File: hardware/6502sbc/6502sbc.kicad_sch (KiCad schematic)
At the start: 1 part, among them U1 W65C02SxP

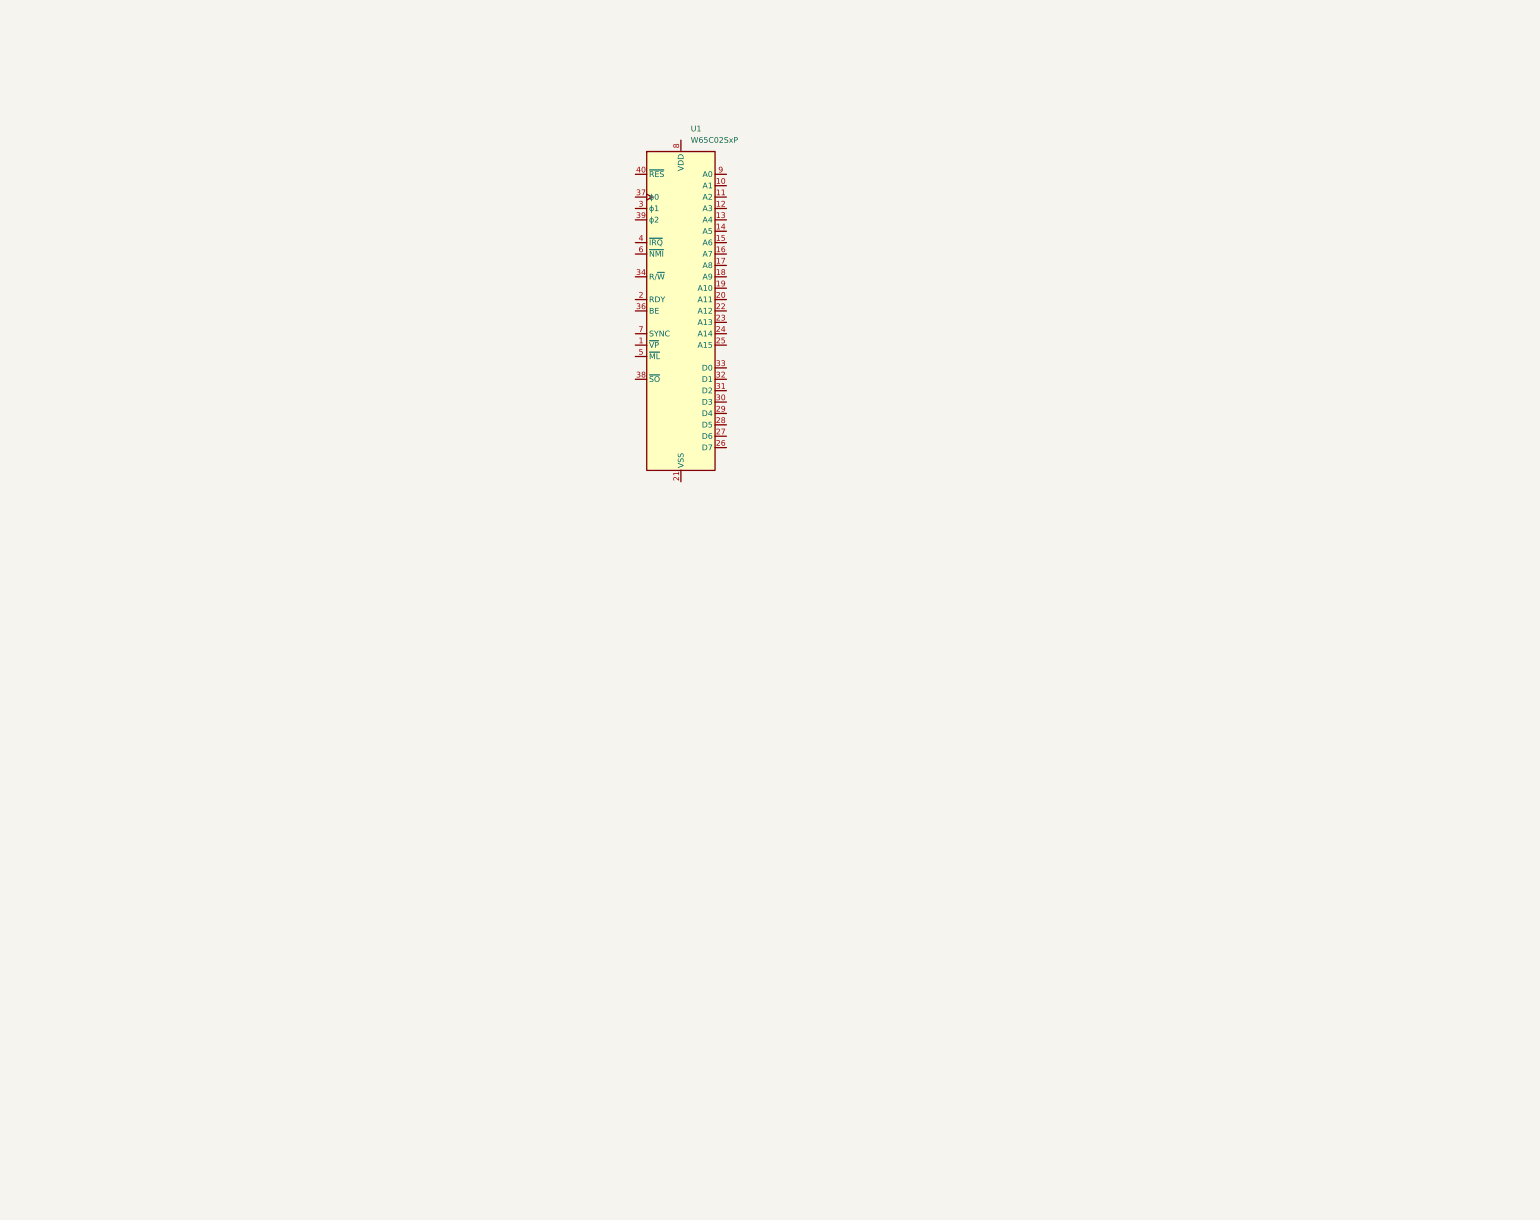
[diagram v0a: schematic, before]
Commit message: KiCAD schematic is mostly complete
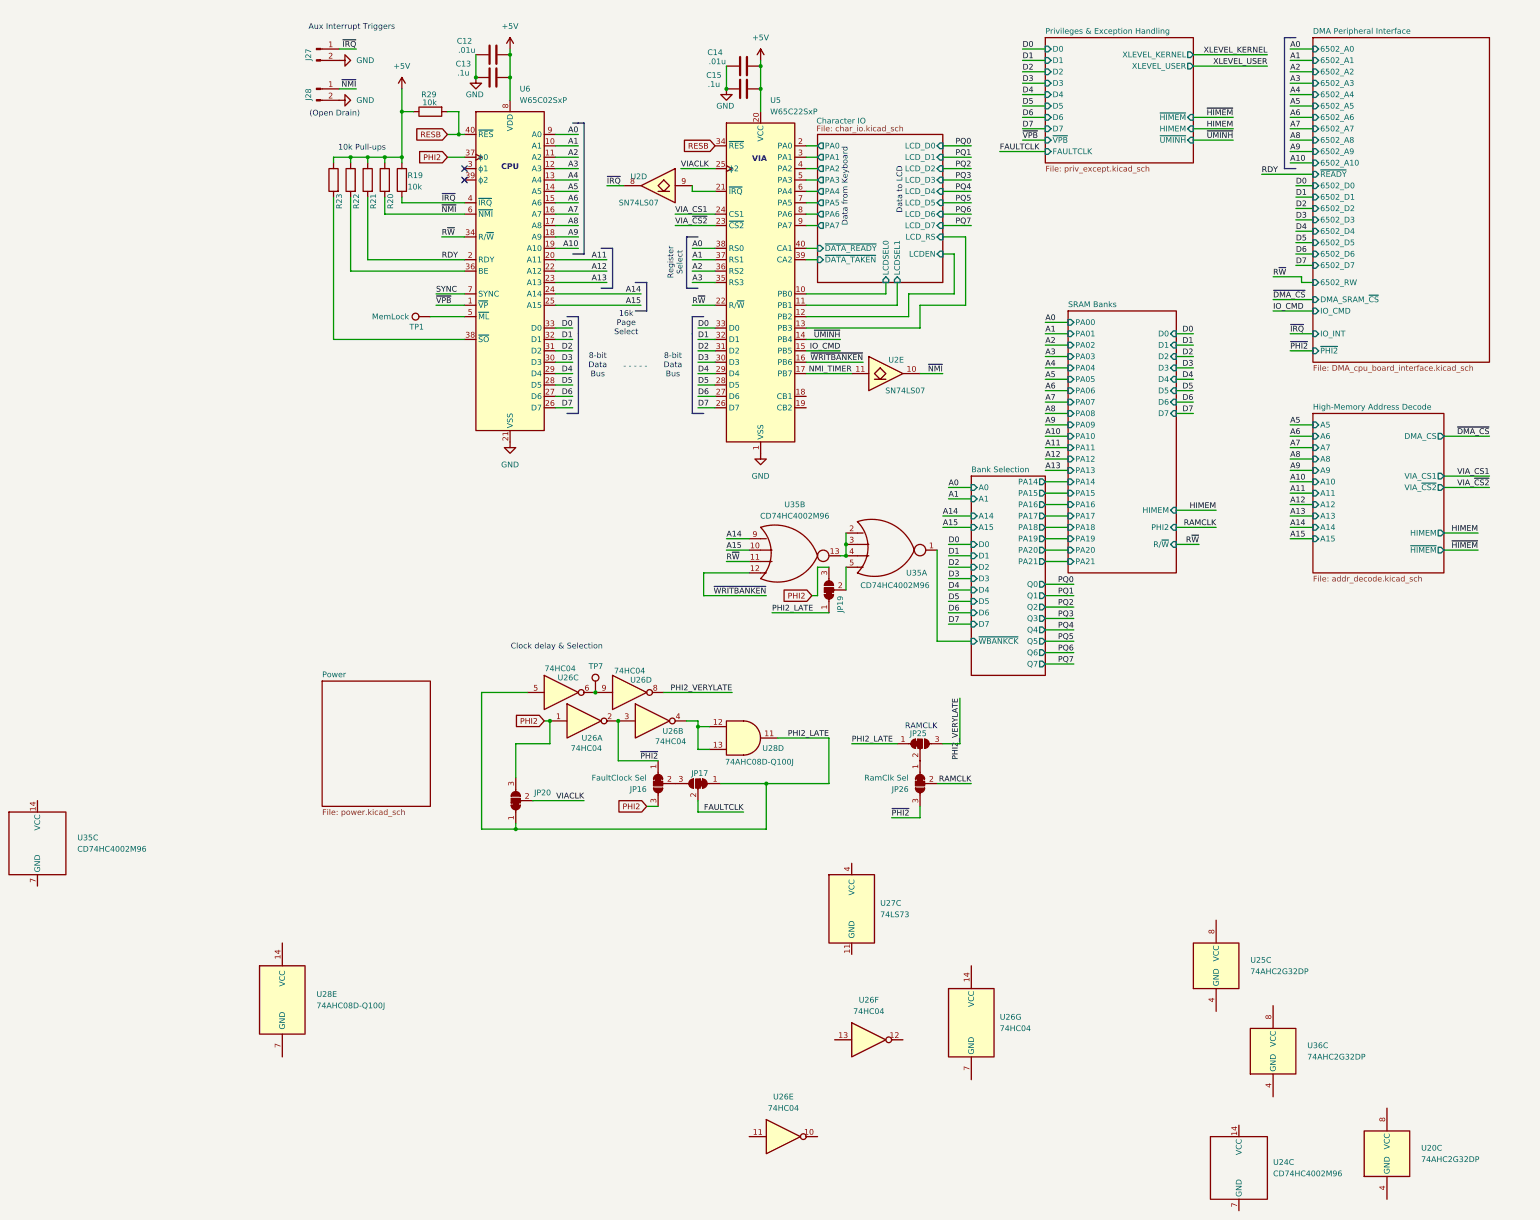
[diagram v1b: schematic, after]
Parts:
- removed U1: W65C02SxP, Package_DIP:DIP-40_W15.24mm, symbol PCM_65xx-library:W65C02SxP
- added C12, C14: .01u, symbol Device:C
- added C13, C15: .1u, symbol Device:C
- added J27, J28: Conn_01x02_Pin, symbol Connector:Conn_01x02_Pin
- added JP16, JP17, JP25: FaultClock Sel, symbol Jumper:SolderJumper_3_Bridged12
- added JP19, JP20: SolderJumper_3_Bridged12, symbol Jumper:SolderJumper_3_Bridged12
- added JP26: RamClk Sel, symbol Jumper:SolderJumper_3_Bridged12
- added R19, R20, R21, R22, R23, R29: 10k, symbol Device:R
- added TP1: MemLock, symbol Connector:TestPoint
- added TP7: TestPoint, symbol Connector:TestPoint
- added U2: SN74LS07, symbol 74xx:SN74LS07
- added U20, U25, U36: 74AHC2G32DP, symbol 74xGxx:74LVC2G32
- added U24, U35: CD74HC4002M96, Package_SO:SOIC-14_3.9x8.7mm_P1.27mm, symbol custom:_1
- added U26: 74HC04, symbol 74xx:74HC04
- added U27: 74LS73, symbol 74xx:74LS73
- added U28: 74AHC08D-Q100J, symbol 74xx:74LS08
- added U5: W65C22SxP, Package_DIP:DIP-40_W15.24mm, symbol PCM_65xx-library:W65C22SxP
- added U6: W65C02SxP, Package_DIP:DIP-40_W15.24mm, symbol PCM_65xx-library:W65C02SxP
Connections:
- new net: TP7.1, U26.6, U26.9
- new net: JP16.2 (C), JP17.3 (B)
- new net: JP25.2 (C), JP26.1 (A)
- new net: R23.2, U6.38 (~{SO})
- new net: U35.13, U35.2, U35.3, U35.4
- new net: U2.9, U5.21 (~{IRQ})
- new net: R22.2, U6.36 (BE)
- new net: TP1.1, U6.5 (~{ML})
- new net: JP19.2 (C), U35.5
- new net: U26.4, U28.12, U28.13
- new net +5V: C12.1, C13.1, C14.1, C15.1, R19.1, R20.1, R21.1, R22.1, R23.1, R29.1, U5.20 (VCC), U6.8 (VDD)
- new net A0: U5.38 (RS0), U6.9 (A0)
- new net A1: U5.37 (RS1), U6.10 (A1)
- new net A10: U6.19 (A10)
- new net A11: U6.20 (A11)
- new net A12: U6.22 (A12)
- new net A13: U6.23 (A13)
- new net A14: U35.9, U6.24 (A14)
- new net A15: U35.10, U6.25 (A15)
- new net A2: U5.36 (RS2), U6.11 (A2)
- new net A3: U5.35 (RS3), U6.12 (A3)
- new net A4: U6.13 (A4)
- new net A5: U6.14 (A5)
- new net A6: U6.15 (A6)
- new net A7: U6.16 (A7)
- new net A8: U6.17 (A8)
- new net A9: U6.18 (A9)
- new net Bank Selection/~{WBANKCK}: U35.1
- new net Character IO/LCDEN: U5.12 (PB2)
- new net Character IO/LCDSEL0: U5.10 (PB0)
- new net Character IO/LCDSEL1: U5.11 (PB1)
- new net Character IO/LCD_RS: U5.13 (PB3)
- new net Character IO/PA0: U5.2 (PA0)
- new net Character IO/PA1: U5.3 (PA1)
- new net Character IO/PA2: U5.4 (PA2)
- new net Character IO/PA3: U5.5 (PA3)
- new net Character IO/PA4: U5.6 (PA4)
- new net Character IO/PA5: U5.7 (PA5)
- new net Character IO/PA6: U5.8 (PA6)
- new net Character IO/PA7: U5.9 (PA7)
- new net Character IO/~{DATA_READY}: U5.40 (CA1)
- new net Character IO/~{DATA_TAKEN}: U5.39 (CA2)
- new net D0: U5.33 (D0), U6.33 (D0)
- new net D1: U5.32 (D1), U6.32 (D1)
- new net D2: U5.31 (D2), U6.31 (D2)
- new net D3: U5.30 (D3), U6.30 (D3)
- new net D4: U5.29 (D4), U6.29 (D4)
- new net D5: U5.28 (D5), U6.28 (D5)
- new net D6: U5.27 (D6), U6.27 (D6)
- new net D7: U5.26 (D7), U6.26 (D7)
- new net FAULTCLK: JP17.2 (C)
- new net GND: C12.2, C13.2, C14.2, C15.2, J27.2 (Pin_2), J28.2 (Pin_2), U5.1 (VSS), U6.21 (VSS)
- new net IO_CMD: U5.15 (PB5)
- new net NMI_TIMER: U2.11, U5.17 (PB7)
- new net PHI2: JP16.3 (B), JP19.3 (B), JP20.3 (B), U26.1, U6.37 (ϕ0)
- new net PHI2_LATE: JP17.1 (A), JP19.1 (A), JP20.1 (A), JP25.1 (A), U26.5, U28.11
- new net PHI2_VERYLATE: JP25.3 (B), U26.8
- new net RAMCLK: JP26.2 (C)
- new net RDY: R21.2, U6.2 (RDY)
- new net RESB: R29.2, U5.34 (~{RES}), U6.40 (~{RES})
- new net R~{W}: U35.11, U5.22 (R/~{W}), U6.34 (R/~{W})
- new net SYNC: U6.7 (SYNC)
- new net VIACLK: JP20.2 (C), U5.25 (ϕ2)
- new net VIA_CS1: U5.24 (CS1)
- new net VIA_~{CS2}: U5.23 (~{CS2})
- new net ~{IRQ}: J27.1 (Pin_1), R19.2, U2.8, U6.4 (~{IRQ})
- new net ~{NMI}: J28.1 (Pin_1), R20.2, U2.10, U6.6 (~{NMI})
- new net ~{PHI2}: JP16.1 (A), JP26.3 (B), U26.2, U26.3
- new net ~{UMINH}: U5.14 (PB4)
- new net ~{VPB}: U6.1 (~{VP})
- new net ~{WRITBANKEN}: U35.12, U5.16 (PB6)
- no-connect marks 0 -> 2
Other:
- added sheet Bank Selection (bank_sel.kicad_sch)
- added sheet Character IO (char_io.kicad_sch)
- added sheet DMA Peripheral Interface (DMA_cpu_board_interface.kicad_sch)
- added sheet High-Memory Address Decode (addr_decode.kicad_sch)
- added sheet Power (power.kicad_sch)
- added sheet Privileges & Exception Handling (priv_except.kicad_sch)
- added sheet SRAM Banks (ram_banks.kicad_sch)
- note added: "(Open Drain)"
- note added: "- - - - -"
- note added: "10k Pull-ups"
- note added: "16k Page Select"
- note added: "8-bit Data Bus"
- note added: "Aux Interrupt Triggers"
- note added: "CPU"
- note added: "Clock delay & Selection"
- note added: "Data from Keyboard"
- note added: "Data to LCD"
- note added: "RAMCLK"
- note added: "Register Select"
- note added: "VIA"
- company: (none) -> Joseph R. Freeston
- title: (none) -> 65c02 Homebrew

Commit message: Preliminary schematic
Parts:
- added D15: LED, symbol Device:LED
- added R78: 510, symbol Device:R
- renumbered C12 to C1, C13 to C2, C14 to C3, C15 to C4, J27 to J1, J28 to J2, JP20 to JP1, JP16 to JP2, JP17 to JP3, JP19 to JP4, JP25 to JP5, JP26 to JP6, R23 to R1, R22 to R2, R21 to R3, R20 to R4, R19 to R5, R29 to R6, TP7 to TP2, U35 to U1, U36 to U10, U20 to U11, U28 to U2, U6 to U3, U26 to U4, U2 to U5, U5 to U6, U27 to U7, U25 to U8, U24 to U9
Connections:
- net +5V: now also R78.1
- net A2: now also U1.2, U2.12
- net PHI2_LATE: now also U4.4; no longer U2.11
- net RESB: now also D15.1 (K)
- net at U1.13, U1.3, U1.4: now also U2.13; no longer U1.2
- net ~{ML}: now reaches TP1.1, U3.5 (~{ML})
- new net: D15.2 (A), R78.2
- new net Bank Selection/WBANKCK2: U2.11
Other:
- sheet Bank Selection ports: added B20, B21, B22, B23, B24, B25, B26, B27, WBANKCK2; removed none
- sheet SRAM Banks ports: added B20, B21, B22, B23, B24, B25, B26, B27, RDY, SYNC, VPB, ~{ML}, ~{NMI}, ~{RESB}; removed none
- note added: "65c02 RESET"
- moved on the sheet: U1B, U2D, U4E, U4F

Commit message: Schematic is nearly done
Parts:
- removed unit 3 of U1
- removed U10, U11, U8: 74AHC2G32DP, symbol 74xGxx:74LVC2G32
- removed unit 5 of U2
- removed unit 7 of U4
- removed U7: 74LS73, symbol 74xx:74LS73
- removed U9: CD74HC4002M96, Package_SO:SOIC-14_3.9x8.7mm_P1.27mm, symbol custom:_1
- added C69, C70: .1u, symbol Device:C
- added J21: Clock input, symbol Connector:Conn_01x02_Pin
- added JP33: Jumper_2_Small_Bridged, symbol Jumper:Jumper_2_Small_Bridged
- added JP34: FaultClock Sel, symbol Jumper:SolderJumper_3_Bridged12
- added R100, R101, R102, R103, R104, R105, R106, R107, R108, R109, R110, R111, R112, R113, R114, R115, R116, R117, R118, R119, R127, R128, R129, R130, R131, R96, R97, R98, R99: 33, symbol Device:R
- added TP10, TP11, TP12, TP8, TP9: TestPoint, symbol Connector:TestPoint
- added U49: 74HC04, Package_SO:SOIC-14_3.9x8.7mm_P1.27mm, symbol 74xx:74HC04
- added U53: 74AHC2G00, symbol 74xGxx:74AHC2G00
- added U54, U55: SN74CBT3245CDBR, symbol custom:SN74CBT3245C
- JP4: value SolderJumper_3_Bridged12 -> FaultClock Sel
- U1: t_pd (ns) (none) -> 8
- U2: footprint (none) -> Package_SO:SOIC-14_3.9x8.7mm_P1.27mm; t_pd (ns) (none) -> 5.9
- U3, U6: footprint Package_DIP:DIP-40_W15.24mm -> Package_LCC:PLCC-44
- U4: footprint (none) -> Package_SO:SOIC-14_3.9x8.7mm_P1.27mm; t_pd (ns) (none) -> 19
- U5: footprint (none) -> Package_SO:SOIC-14_3.9x8.7mm_P1.27mm; t_pd (ns) (none) -> 30
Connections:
- net +5V: now also C69.1, C70.1, U54.20 (VCC), U55.20 (VCC)
- net A0: now also R104.2; no longer U3.9 (A0)
- net A1: now also R105.2; no longer U3.10 (A1)
- net A10: now also R114.2; no longer U3.19 (A10)
- net A11: now also R115.2; no longer U3.20 (A11)
- net A12: now also R116.2; no longer U3.22 (A12)
- net A13: now also R117.2; no longer U3.23 (A13)
- net A14: now also R118.2; no longer U1.9, U3.24 (A14)
- net A15: now also R119.2; no longer U3.25 (A15)
- net A2: now also R106.2, U49.13; no longer U1.2, U3.11 (A2)
- net A3: now also R107.2; no longer U3.12 (A3)
- net A4: now also R108.2; no longer U3.13 (A4)
- net A5: now also R109.2; no longer U3.14 (A5)
- net A6: now also R110.2; no longer U3.15 (A6)
- net A7: now also R111.2; no longer U3.16 (A7)
- net A8: now also R112.2; no longer U3.17 (A8)
- net A9: now also R113.2; no longer U3.18 (A9)
- net Bank Selection/~{WBANKCK}: now also U53.7; no longer U1.1
- net D0: now also R96.2, U54.2 (A1), U55.2 (A1); no longer U3.33 (D0)
- net D1: now also R97.2, U54.3 (A2), U55.3 (A2); no longer U3.32 (D1)
- net D2: now also R98.2, U54.4 (A3), U55.4 (A3); no longer U3.31 (D2)
- net D3: now also R99.2, U54.5 (A4), U55.5 (A4); no longer U3.30 (D3)
- net D4: now also R100.2, U54.6 (A5), U55.6 (A5); no longer U3.29 (D4)
- net D5: now also R101.2, U54.7 (A6), U55.7 (A6); no longer U3.28 (D5)
- net D6: now also R102.2, U54.8 (A7), U55.8 (A7); no longer U3.27 (D6)
- net D7: now also R103.2, U54.9 (A8), U55.9 (A8); no longer U3.26 (D7)
- net FAULTCLK: now also R128.2; no longer JP3.2 (C)
- net GND: now also C69.2, C70.2, J21.2 (Pin_2), JP33.1 (A), U54.10 (GND), U55.10 (GND)
- net PHI2: now also U1.2, U1.3, U1.4, U1.5, U4.13, J21.1 (Pin_1), TP8.1; no longer JP2.3 (B), JP4.3 (B), U4.1
- net PHI2_LATE: now also TP9.1, U53.3; no longer JP4.1 (A), U4.4, U4.5
- net PHI2_VERYLATE: now also JP2.3 (B), TP2.1, U4.2, U4.3; no longer U4.8
- net RAMCLK: now also R127.2; no longer JP6.2 (C)
- net R~{W}: now also R131.1; no longer U3.34 (R/~{W})
- net VIACLK: now also R129.2; no longer JP1.2 (C)
- net ~{PHI2}: now also U1.1, U1.9, U4.1, JP34.3 (B), U53.5, U53.6; no longer U4.2, U4.3
- net ~{PHI2_LATE}: now reaches U4.12
- net ~{PHI2_LATE}: now also JP4.1 (A), U4.5
- net at U1.13, U2.13: now also U53.1; no longer U1.3, U1.4
- net at JP4.2 (C): now also JP34.1 (A); no longer U1.5
- net at U4.10: now also U4.9, TP11.1
- net at U4.11: now also JP33.2 (B)
- new net: JP1.2 (C), R129.1
- new net: R105.1, U3.10 (A1)
- new net: R102.1, U3.27 (D6)
- new net: R106.1, U3.11 (A2)
- new net: JP6.2 (C), R127.1
- new net: R118.1, U3.24 (A14)
- new net: TP10.1, U4.6
- new net: JP34.2 (C), R130.1
- new net: R119.1, U3.25 (A15)
- new net: R104.1, U3.9 (A0)
- new net: TP12.1, U4.8
- new net: JP3.2 (C), R128.1
- new net: R107.1, U3.12 (A3)
- new net: R108.1, U3.13 (A4)
- new net: R109.1, U3.14 (A5)
- new net: R110.1, U3.15 (A6)
- new net: R111.1, U3.16 (A7)
- new net: R112.1, U3.17 (A8)
- new net: R113.1, U3.18 (A9)
- new net: R114.1, U3.19 (A10)
- new net: R115.1, U3.20 (A11)
- new net: R116.1, U3.22 (A12)
- new net: R117.1, U3.23 (A13)
- new net: R103.1, U3.26 (D7)
- new net: R101.1, U3.28 (D5)
- new net: R100.1, U3.29 (D4)
- new net: R99.1, U3.30 (D3)
- new net: R98.1, U3.31 (D2)
- new net: R97.1, U3.32 (D1)
- new net: R96.1, U3.33 (D0)
- new net: R131.2, U3.34 (R/~{W})
- new net: U49.12, U53.2
- new net DMA Peripheral Interface/6502_D0: U55.18 (B1)
- new net DMA Peripheral Interface/6502_D1: U55.17 (B2)
- new net DMA Peripheral Interface/6502_D2: U55.16 (B3)
- new net DMA Peripheral Interface/6502_D3: U55.15 (B4)
- new net DMA Peripheral Interface/6502_D4: U55.14 (B5)
- new net DMA Peripheral Interface/6502_D5: U55.13 (B6)
- new net DMA Peripheral Interface/6502_D6: U55.12 (B7)
- new net DMA Peripheral Interface/6502_D7: U55.11 (B8)
- new net PHI2_BUSR: R130.2, U54.19 (~{OE}), U55.19 (~{OE})
- new net SRAM Banks/D0: U54.18 (B1)
- new net SRAM Banks/D1: U54.17 (B2)
- new net SRAM Banks/D2: U54.16 (B3)
- new net SRAM Banks/D3: U54.15 (B4)
- new net SRAM Banks/D4: U54.14 (B5)
- new net SRAM Banks/D5: U54.13 (B6)
- new net SRAM Banks/D6: U54.12 (B7)
- new net SRAM Banks/D7: U54.11 (B8)
- new net ~{PHI2_LATER}: JP4.3 (B), U4.4
- no-connect marks 2 -> 4
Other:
- note added: "- - -"
- note added: "Unused NOT gates with provisions to use them in rework"
- note added: "Voltage Regulators, Power inputs, and the like"
- note removed: "- - - - -"
- moved on the sheet: J1, J2, JP2, R78, TP2, U1A, U1B, U4A, U4B, U4C, U4D, U4E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
